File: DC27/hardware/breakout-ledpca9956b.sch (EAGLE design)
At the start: 34 parts, among them IC1 PCA9956BTWY, J1 top-bot-connector

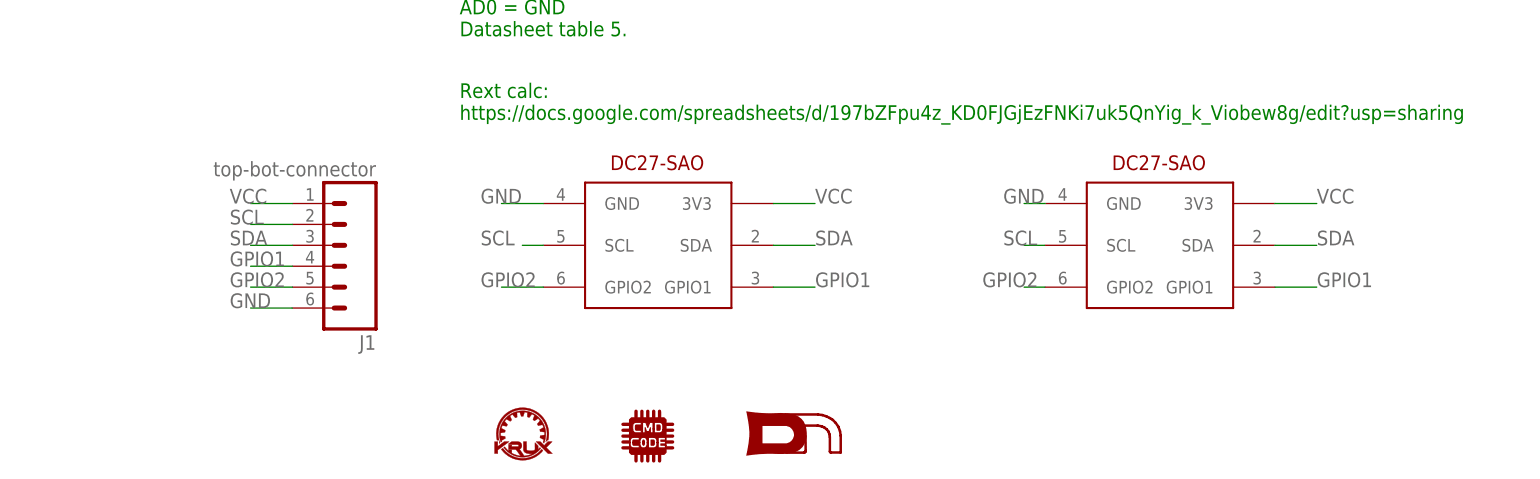
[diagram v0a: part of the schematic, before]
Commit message: top board farther, made a breakout board for new led driver
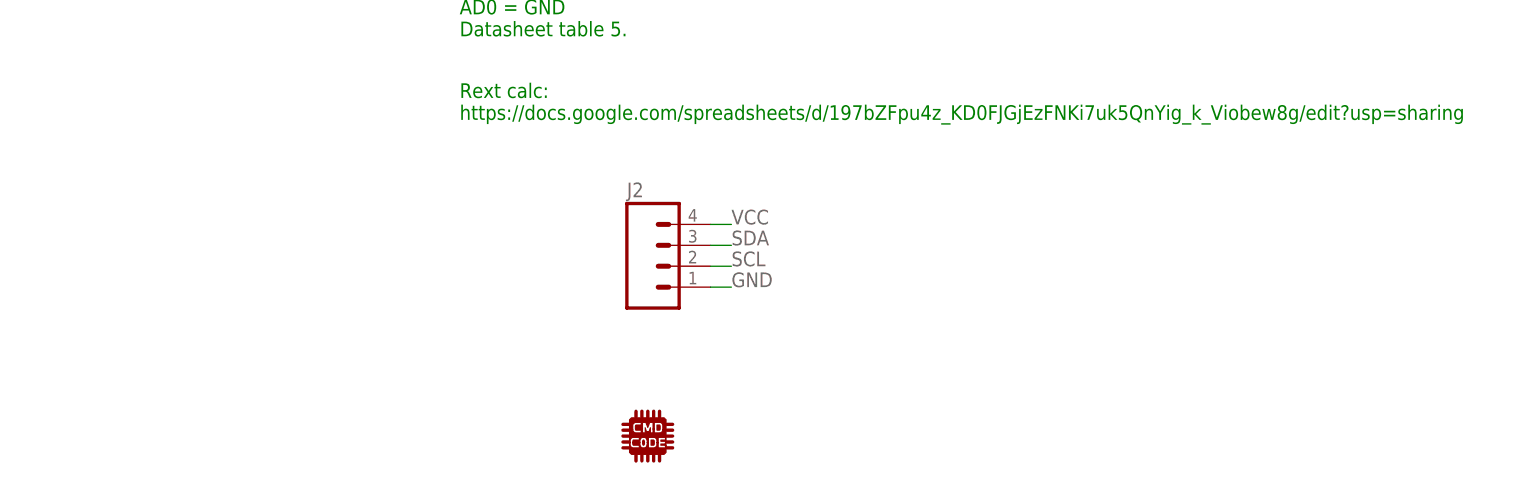
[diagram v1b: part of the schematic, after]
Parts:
- removed J1: top-bot-connector, connector:M06SILK_FEMALE_PTH
- removed U$1: KRUX_LOGO, darknet_parts_library:KRUX_LOGO
- removed U$3, U$4: DC-27-SAO, defcon:DC-27-SAO
- removed U$5: DN_LOGODC26, logos:DN_LOGODC26
- added J2: (no value), connector:M04PTH
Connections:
- removed net GPIO1: J1.4, U$3.GPIO1, U$4.GPIO1
- removed net GPIO2: J1.5, U$3.GPIO2, U$4.GPIO2
- net GND: now also J2.1; no longer J1.6, U$3.GND, U$4.GND
- net SCL: now also J2.2; no longer J1.2, U$3.SCL, U$4.SCL
- net SDA: now also J2.3; no longer J1.3, U$3.SDA, U$4.SDA
- net VCC: now also J2.4; no longer J1.1, U$3.3V3, U$4.3V3
